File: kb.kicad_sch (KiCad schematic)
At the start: 185 parts, among them J1 Conn_02x04, J2 10029449-001RLF, J3 Conn_01x05, J4 Conn_01x10, J5 Conn_01x07, SW1 RotaryEncoder_Switch, U1 Pico, U2 SN74AHCT125D

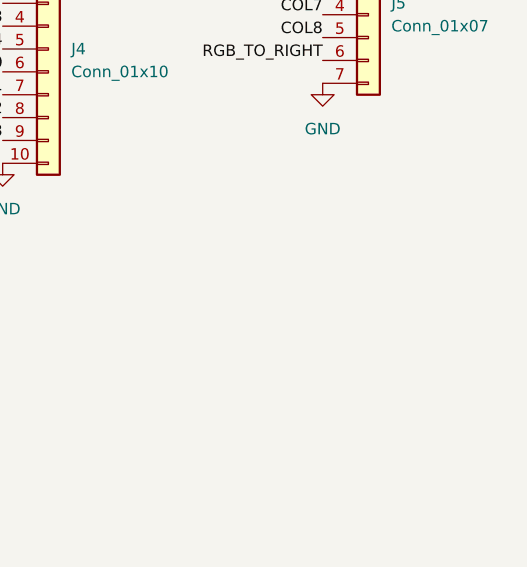
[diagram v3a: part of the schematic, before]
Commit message: add silkscreens, power port
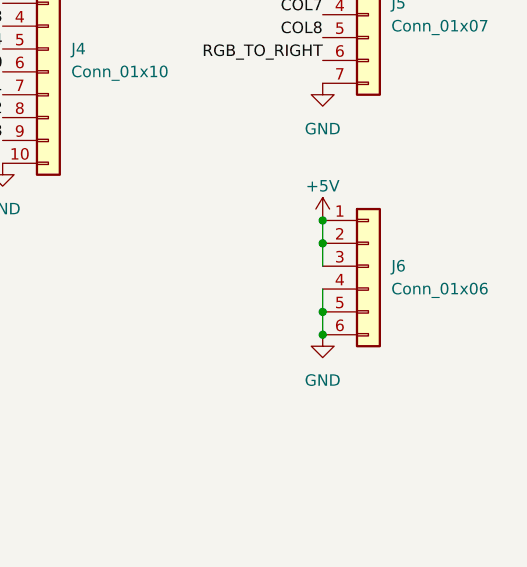
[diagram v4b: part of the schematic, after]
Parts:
- added J6: Conn_01x06, Connector_PinHeader_2.54mm:PinHeader_1x06_P2.54mm_Vertical, symbol Connector_Generic:Conn_01x06
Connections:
- net +5V: now also J6.1 (Pin_1), J6.2 (Pin_2), J6.3 (Pin_3)
- net GND: now also J6.4 (Pin_4), J6.5 (Pin_5), J6.6 (Pin_6)
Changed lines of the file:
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@@
   (junction (at 228.6 123.19) (diameter 0) (color 0 0 0 0)
   )
+  (junction (at 388.62 223.52) (diameter 0) (color 0 0 0 0)
+  )
   (junction (at 107.95 36.83) (diameter 0) (color 0 0 0 0)
   )
+  (junction (at 388.62 233.68) (diameter 0) (color 0 0 0 0)
+  )
   (junction (at 228.6 163.83) (diameter 0) (color 0 0 0 0)
   )
@@
   (junction (at 279.4 161.29) (diameter 0) (color 0 0 0 0)
   )
+  (junction (at 388.62 220.98) (diameter 0) (color 0 0 0 0)
+  )
   (junction (at 52.07 189.23) (diameter 0) (color 0 0 0 0)
   )
@@
   (junction (at 196.85 123.19) (diameter 0) (color 0 0 0 0)
   )
+  (junction (at 388.62 231.14) (diameter 0) (color 0 0 0 0)
+  )
   (junction (at 101.6 245.11) (diameter 0) (color 0 0 0 0)
   )
@@
     (stroke (width 0) (type default) (color 0 0 0 0))
   )
+  (wire (pts (xy 388.62 231.14) (xy 388.62 233.68))
+    (stroke (width 0) (type default) (color 0 0 0 0))
+  )
   (wire (pts (xy 172.72 256.54) (xy 189.23 256.54))
     (stroke (width 0) (type default) (color 0 0 0 0))
@@
     (stroke (width 0) (type default) (color 0 0 0 0))
   )
+  (wire (pts (xy 388.62 223.52) (xy 388.62 226.06))
+    (stroke (width 0) (type default) (color 0 0 0 0))
+  )
   (wire (pts (xy 184.15 201.93) (xy 184.15 242.57))
     (stroke (width 0) (type default) (color 0 0 0 0))
@@
     (stroke (width 0) (type default) (color 0 0 0 0))
   )
+  (wire (pts (xy 388.62 228.6) (xy 388.62 231.14))
+    (stroke (width 0) (type default) (color 0 0 0 0))
+  )
   (wire (pts (xy 133.35 82.55) (xy 133.35 86.36))
     (stroke (width 0) (type default) (color 0 0 0 0))
@@
     (stroke (width 0) (type default) (color 0 0 0 0))
   )
+  (wire (pts (xy 388.62 220.98) (xy 388.62 223.52))
+    (stroke (width 0) (type default) (color 0 0 0 0))
+  )
   (wire (pts (xy 107.95 34.29) (xy 107.95 36.83))
     (stroke (width 0) (type default) (color 0 0 0 0))
@@
     (pin "2")
   )
+  (symbol (lib_id "power:GND") (at 388.62 233.68 0) (unit 1)
+    (in_bom yes) (on_board yes) (fields_autoplaced)
+    (property "Reference" "#PWR06" (id 0) (at 388.62 240.03 0)
+      (effects (font (size 1.27 1.27)) hide)
+    )
+    (property "Value" "GND" (id 1) (at 388.62 238.76 0))
+    (property "Footprint" "" (id 2) (at 388.62 233.68 0)
+      (effects (font (size 1.27 1.27)) hide)
+    )
+    (property "Datasheet" "" (id 3) (at 388.62 233.68 0)
+      (effects (font (size 1.27 1.27)) hide)
+    )
+    (pin "1")
+  )
   (symbol (lib_id "power:+5V") (at 69.85 82.55 0) (unit 1)
     (in_bom yes) (on_board yes) (fields_autoplaced)
@@
     (pin "2")
   )
+  (symbol (lib_id "power:+5V") (at 388.62 220.98 0) (unit 1)
+    (in_bom yes) (on_board yes)
+    (property "Reference" "#PWR05" (id 0) (at 388.62 224.79 0)
+      (effects (font (size 1.27 1.27)) hide)
+    )
+    (property "Value" "+5V" (id 1) (at 388.62 217.17 0))
+    (property "Footprint" "" (id 2) (at 388.62 220.98 0)
+      (effects (font (size 1.27 1.27)) hide)
+    )
+    (property "Datasheet" "" (id 3) (at 388.62 220.98 0)
+      (effects (font (size 1.27 1.27)) hide)
+    )
+    (pin "1")
+  )
   (symbol (lib_id "power:GND") (at 302.26 204.47 0) (unit 1)
     (in_bom yes) (on_board yes)
@@
     (pin "1")
   )
+  (symbol (lib_id "Connector_Generic:Conn_01x06") (at 393.7 226.06 0) (unit 1)
+    (in_bom yes) (on_board yes)
+    (property "Reference" "J6" (id 0) (at 396.24 226.06 0)
+      (effects (font (size 1.27 1.27)) (justify left))
+    )
+    (property "Value" "Conn_01x06" (id 1) (at 396.24 228.6 0)
+      (effects (font (size 1.27 1.27)) (justify left))
+    )
+    (property "Footprint" "Connector_PinHeader_2.54mm:PinHeader_1x06_P2.54mm_Vertical" (id 2) (at 393.7 226.06 0)
+      (effects (font (size 1.27 1.27)) hide)
+    )
+    (property "Datasheet" "~" (id 3) (at 393.7 226.06 0)
+      (effects (font (size 1.27 1.27)) hide)
+    )
+    (pin "1")
+    (pin "2")
+    (pin "3")
+    (pin "4")
+    (pin "5")
+    (pin "6")
+  )
   (symbol (lib_id "Device:D_Small") (at 52.07 146.05 90) (unit 1)
     (in_bom yes) (on_board yes)
@@
       (reference "#PWR04") (unit 1) (value "GND") (footprint "")
     )
+    (path "/4ed14abc-dbd0-45bc-8acf-3f88e8825706"
+      (reference "#PWR05") (unit 1) (value "+5V") (footprint "")
+    )
+    (path "/40fb6619-4c3d-4a08-8048-fae297650007"
+      (reference "#PWR06") (unit 1) (value "GND") (footprint "")
+    )
     (path "/53f67357-c441-4e08-a422-cc01051c969e"
       (reference "#PWR07") (unit 1) (value "GND") (footprint "")
@@
       (reference "J5") (unit 1) (value "Conn_01x07") (footprint "Connector_PinHeader_2.54mm:PinHeader_1x07_P2.54mm_Vertical")
     )
+    (path "/a252f866-89e7-4b0c-a051-b3d9be2a2683"
+      (reference "J6") (unit 1) (value "Conn_01x06") (footprint "Connector_PinHeader_2.54mm:PinHeader_1x06_P2.54mm_Vertical")
+    )
     (path "/8a089bf5-08f1-41ee-aa36-391f5cdf0f9d"

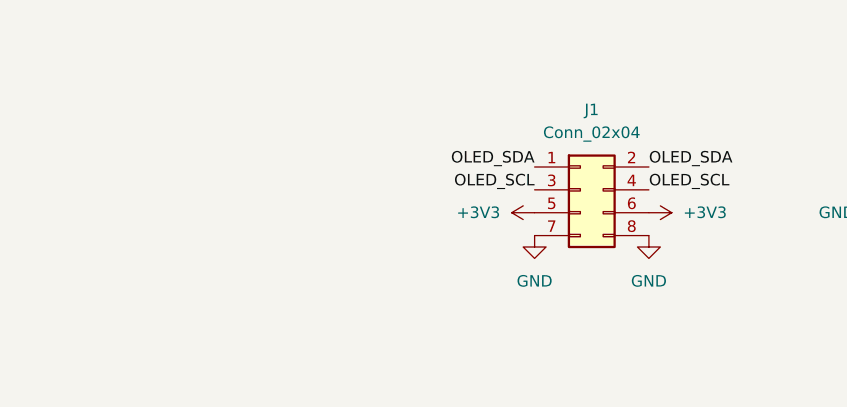
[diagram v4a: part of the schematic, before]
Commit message: Add pullup i2c
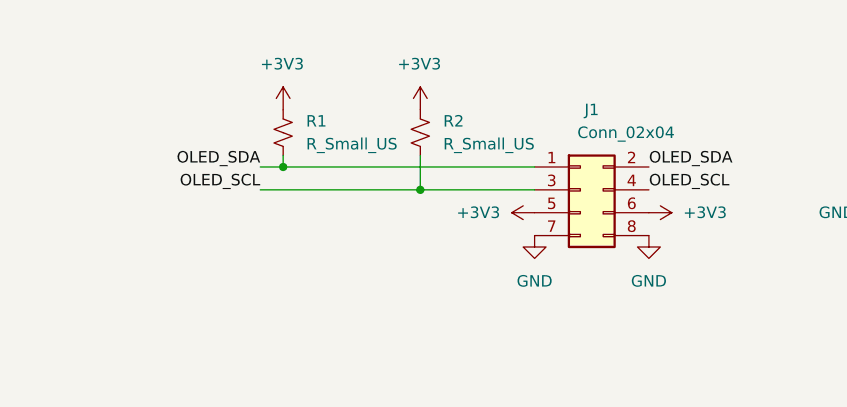
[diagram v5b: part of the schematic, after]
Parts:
- added R1, R2: R_Small_US, Resistor_SMD:R_0805_2012Metric_Pad1.20x1.40mm_HandSolder, symbol Device:R_Small_US
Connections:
- net +3V3: now also R1.1, R2.1
- net OLED_SCL: now also R2.2
- net OLED_SDA: now also R1.2
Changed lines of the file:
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@@
   (junction (at 179.07 270.51) (diameter 0) (color 0 0 0 0)
   )
+  (junction (at 209.55 29.21) (diameter 0) (color 0 0 0 0)
+  )
   (junction (at 107.95 29.21) (diameter 0) (color 0 0 0 0)
   )
@@
   (junction (at 210.82 107.95) (diameter 0) (color 0 0 0 0)
   )
+  (junction (at 224.79 31.75) (diameter 0) (color 0 0 0 0)
+  )
   (junction (at 196.85 82.55) (diameter 0) (color 0 0 0 0)
   )
@@
     (stroke (width 0) (type default) (color 0 0 0 0))
   )
+  (wire (pts (xy 207.01 29.21) (xy 209.55 29.21))
+    (stroke (width 0) (type default) (color 0 0 0 0))
+  )
   (wire (pts (xy 45.72 215.9) (xy 62.23 215.9))
     (stroke (width 0) (type default) (color 0 0 0 0))
@@
     (stroke (width 0) (type default) (color 0 0 0 0))
   )
+  (wire (pts (xy 224.79 27.94) (xy 224.79 31.75))
+    (stroke (width 0) (type default) (color 0 0 0 0))
+  )
   (wire (pts (xy 152.4 161.29) (xy 152.4 201.93))
     (stroke (width 0) (type default) (color 0 0 0 0))
@@
     (stroke (width 0) (type default) (color 0 0 0 0))
   )
+  (wire (pts (xy 207.01 31.75) (xy 224.79 31.75))
+    (stroke (width 0) (type default) (color 0 0 0 0))
+  )
   (wire (pts (xy 292.1 123.19) (xy 292.1 127))
     (stroke (width 0) (type default) (color 0 0 0 0))
@@
     (stroke (width 0) (type default) (color 0 0 0 0))
   )
+  (wire (pts (xy 224.79 31.75) (xy 237.49 31.75))
+    (stroke (width 0) (type default) (color 0 0 0 0))
+  )
   (wire (pts (xy 26.67 175.26) (xy 30.48 175.26))
     (stroke (width 0) (type default) (color 0 0 0 0))
@@
     (stroke (width 0) (type default) (color 0 0 0 0))
   )
+  (wire (pts (xy 209.55 27.94) (xy 209.55 29.21))
+    (stroke (width 0) (type default) (color 0 0 0 0))
+  )
   (wire (pts (xy 388.62 220.98) (xy 388.62 223.52))
     (stroke (width 0) (type default) (color 0 0 0 0))
@@
     (stroke (width 0) (type default) (color 0 0 0 0))
   )
+  (wire (pts (xy 209.55 29.21) (xy 237.49 29.21))
+    (stroke (width 0) (type default) (color 0 0 0 0))
+  )
   (wire (pts (xy 204.47 204.47) (xy 207.01 204.47))
     (stroke (width 0) (type default) (color 0 0 0 0))
@@
     (effects (font (size 1.27 1.27)) (justify left bottom))
   )
-  (label "OLED_SCL" (at 237.49 31.75 180)
+  (label "OLED_SCL" (at 207.01 31.75 180)
     (effects (font (size 1.27 1.27)) (justify right bottom))
   )
@@
     (effects (font (size 1.27 1.27)) (justify right bottom))
   )
-  (label "OLED_SDA" (at 237.49 29.21 180)
+  (label "OLED_SDA" (at 207.01 29.21 180)
     (effects (font (size 1.27 1.27)) (justify right bottom))
   )
@@
     (effects (font (size 1.27 1.27)) (justify right bottom))
   )
+  (symbol (lib_id "Device:R_Small_US") (at 209.55 25.4 0) (unit 1)
+    (in_bom yes) (on_board yes) (fields_autoplaced)
+    (property "Reference" "R1" (id 0) (at 212.09 24.1299 0)
+      (effects (font (size 1.27 1.27)) (justify left))
+    )
+    (property "Value" "R_Small_US" (id 1) (at 212.09 26.6699 0)
+      (effects (font (size 1.27 1.27)) (justify left))
+    )
+    (property "Footprint" "Resistor_SMD:R_0805_2012Metric_Pad1.20x1.40mm_HandSolder" (id 2) (at 209.55 25.4 0)
+      (effects (font (size 1.27 1.27)) hide)
+    )
+    (property "Datasheet" "~" (id 3) (at 209.55 25.4 0)
+      (effects (font (size 1.27 1.27)) hide)
+    )
+    (pin "1")
+    (pin "2")
+  )
   (symbol (lib_id "Device:D_Small") (at 179.07 186.69 90) (unit 1)
     (in_bom yes) (on_board yes)
@@
   )
   (symbol (lib_id "Connector_Generic:Conn_02x04_Odd_Even") (at 242.57 31.75 0) (unit 1)
-    (in_bom yes) (on_board yes) (fields_autoplaced)
+    (in_bom yes) (on_board yes)
     (property "Reference" "J1" (id 0) (at 243.84 22.86 0))
-    (property "Value" "Conn_02x04" (id 1) (at 243.84 25.4 0))
+    (property "Value" "Conn_02x04" (id 1) (at 247.65 25.4 0))
     (property "Footprint" "Connector_PinHeader_2.54mm:PinHeader_2x04_P2.54mm_Vertical" (id 2) (at 242.57 31.75 0)
       (effects (font (size 1.27 1.27)) hide)
@@
     (pin "2")
   )
+  (symbol (lib_id "power:+3V3") (at 224.79 22.86 0) (unit 1)
+    (in_bom yes) (on_board yes)
+    (property "Reference" "#PWR010" (id 0) (at 224.79 26.67 0)
+      (effects (font (size 1.27 1.27)) hide)
+    )
+    (property "Value" "+3V3" (id 1) (at 222.25 17.78 0)
+      (effects (font (size 1.27 1.27)) (justify left))
+    )
+    (property "Footprint" "" (id 2) (at 224.79 22.86 0)
+      (effects (font (size 1.27 1.27)) hide)
+    )
+    (property "Datasheet" "" (id 3) (at 224.79 22.86 0)
+      (effects (font (size 1.27 1.27)) hide)
+    )
+    (pin "1")
+  )
   (symbol (lib_id "MX_Alps_Hybrid:MX-NoLED") (at 243.84 121.92 0) (unit 1)
     (in_bom yes) (on_board yes) (fields_autoplaced)
@@
     (pin "2")
   )
+  (symbol (lib_id "Device:R_Small_US") (at 224.79 25.4 0) (unit 1)
+    (in_bom yes) (on_board yes) (fields_autoplaced)
+    (property "Reference" "R2" (id 0) (at 227.33 24.1299 0)
+      (effects (font (size 1.27 1.27)) (justify left))
+    )
+    (property "Value" "R_Small_US" (id 1) (at 227.33 26.6699 0)
+      (effects (font (size 1.27 1.27)) (justify left))
+    )
+    (property "Footprint" "Resistor_SMD:R_0805_2012Metric_Pad1.20x1.40mm_HandSolder" (id 2) (at 224.79 25.4 0)
+      (effects (font (size 1.27 1.27)) hide)
+    )
+    (property "Datasheet" "~" (id 3) (at 224.79 25.4 0)
+      (effects (font (size 1.27 1.27)) hide)
+    )
+    (pin "1")
+    (pin "2")
+  )
   (symbol (lib_id "MX_Alps_Hybrid:MX-NoLED") (at 275.59 203.2 0) (unit 1)
     (in_bom yes) (on_board yes) (fields_autoplaced)
@@
     (pin "1")
   )
+  (symbol (lib_id "power:+3V3") (at 209.55 22.86 0) (unit 1)
+    (in_bom yes) (on_board yes)
+    (property "Reference" "#PWR09" (id 0) (at 209.55 26.67 0)
+      (effects (font (size 1.27 1.27)) hide)
+    )
+    (property "Value" "+3V3" (id 1) (at 207.01 17.78 0)
+      (effects (font (size 1.27 1.27)) (justify left))
+    )
+    (property "Footprint" "" (id 2) (at 209.55 22.86 0)
+      (effects (font (size 1.27 1.27)) hide)
+    )
+    (property "Datasheet" "" (id 3) (at 209.55 22.86 0)
+      (effects (font (size 1.27 1.27)) hide)
+    )
+    (pin "1")
+  )
   (symbol (lib_id "power:GND") (at 302.26 204.47 0) (unit 1)
     (in_bom yes) (on_board yes)
@@
       (reference "#PWR08") (unit 1) (value "GND") (footprint "")
     )
+    (path "/50cc7bf8-024c-4d0b-969e-3c8fcee99729"
+      (reference "#PWR09") (unit 1) (value "+3V3") (footprint "")
+    )
+    (path "/2f0f5b54-186f-4256-9577-cdf416d1f7f4"
+      (reference "#PWR010") (unit 1) (value "+3V3") (footprint "")
+    )
     (path "/5203f11e-8e72-4adf-97a9-3edc8d99facc"
       (reference "#PWR012") (unit 1) (value "GND") (footprint "")
@@
       (reference "MX44") (unit 1) (value "MX-NoLED") (footprint "MX_Only:MXOnly-1U-Hotswap")
     )
+    (path "/00ec8f69-8fd7-432c-a32b-167b6504af5d"
+      (reference "R1") (unit 1) (value "R_Small_US") (footprint "Resistor_SMD:R_0805_2012Metric_Pad1.20x1.40mm_HandSolder")
+    )
+    (path "/398f6422-bd79-4c3a-820b-5eb71067ed84"
+      (reference "R2") (unit 1) (value "R_Small_US") (footprint "Resistor_SMD:R_0805_2012Metric_Pad1.20x1.40mm_HandSolder")
+    )
     (path "/d7cdbb55-f97a-4907-9bdc-aa8d09aa31fb"

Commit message: add new level shifter, add component values
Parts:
- removed U2: SN74AHCT125D, Package_SO:TSSOP-14-1EP_4.4x5mm_P0.65mm, symbol SN74AHCT125D:SN74AHCT125D
- added C45, C46: 0.1uF, Capacitor_SMD:C_0805_2012Metric_Pad1.18x1.45mm_HandSolder, symbol Device:C_Small
- added U2: TXB0101DBVR, TXB0101DBVR:SOT65P210X110-6N, symbol TXB0101DBVR:TXB0101DBVR
- C1, C2: value C_Small -> 0.1uF
- C10, C11, C12, C13, C14, C15, C16, C17, C18, C19, C20, C21, C22, C23, C24, C25, C26, C27, C28, C29, C3, C30, C31, C32, C33, C34, C35, C36, C37, C38, C39, C4, C40, C41, C42, C43, C44, C5, C6, C7, C8, C9: value C_Small -> 0.1nF
- R1, R2: value R_Small_US -> 4.7k
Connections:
- net +3V3: now also C45.1, U2.1 (VCCA), U2.5 (OE)
- net +5V: now also C46.1, U2.6 (VCCB)
- net GND: now also C45.2, C46.2, U2.2 (GND)
- net RGB_3V3: now also U2.3 (A)
- net RGB_5V: now also U2.4 (B)

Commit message: fix component values
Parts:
- C10, C11, C12, C13, C14, C15, C16, C17, C18, C19, C20, C21, C22, C23, C24, C25, C26, C27, C28, C29, C3, C30, C31, C32, C33, C34, C35, C36, C37, C38, C39, C4, C40, C41, C42, C43, C44, C5, C6, C7, C8, C9: value 0.1nF -> 0.1uF
